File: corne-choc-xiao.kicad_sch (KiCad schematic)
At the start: 46 parts, among them J1 LiPo, Q1 SI2032, SW10 SW_PUSH, SW11 SW_PUSH, SW12 SW_PUSH, SW14 SW_PUSH, SW15 SW_PUSH, SW16 SW_PUSH, SW17 SW_PUSH, SW18 SW_PUSH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

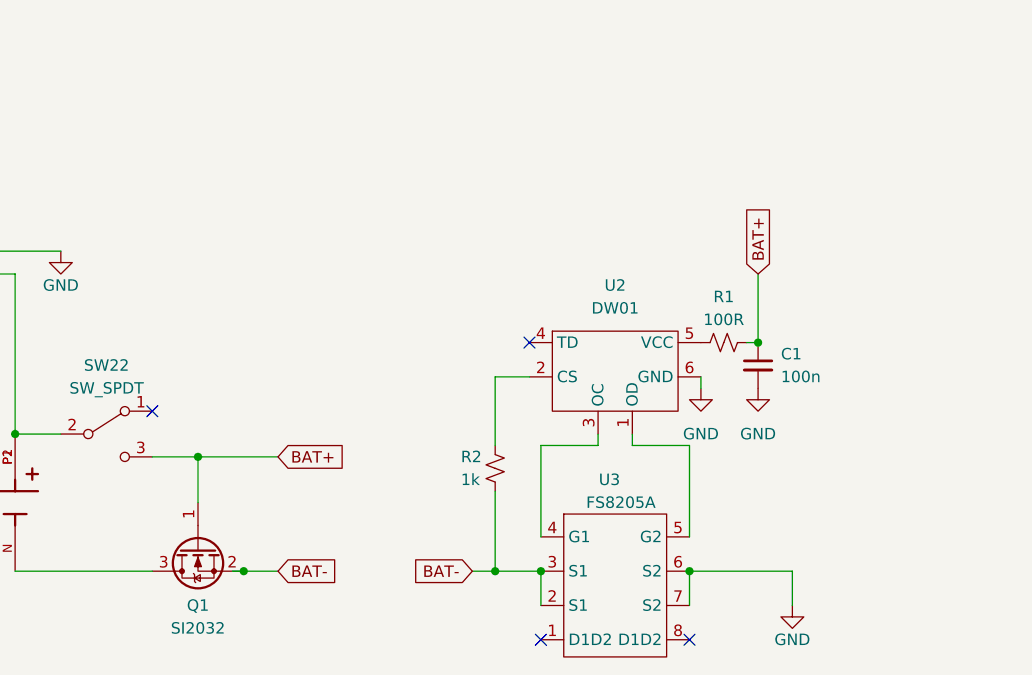
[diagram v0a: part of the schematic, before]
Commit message: fix battery protection circuit
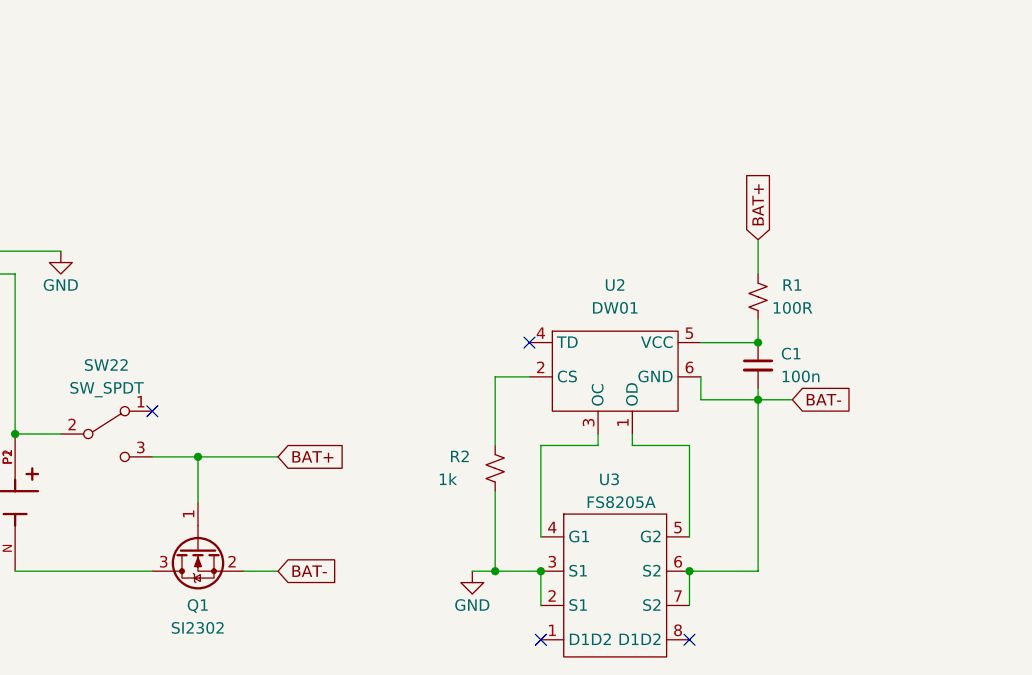
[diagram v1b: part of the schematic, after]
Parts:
- Q1: value SI2032 -> SI2302
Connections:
- net BAT+: no longer C1.1
- net BAT-: now also C1.2, U2.6 (GND), U3.6 (S2), U3.7 (S2); no longer R2.2, U3.2 (S1), U3.3 (S1)
- net GND: now also R2.2, U3.2 (S1), U3.3 (S1); no longer C1.2, U2.6 (GND), U3.6 (S2), U3.7 (S2)
- net at R1.1, U2.5 (VCC): now also C1.1
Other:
- moved on the sheet: R1

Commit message: added readme and ibom
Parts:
- renumbered SW22 to S1
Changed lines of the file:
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@@
   (symbol (lib_id "Switch:SW_SPDT") (at 50.8 134.62 0) (unit 1)
     (in_bom yes) (on_board yes) (dnp no) (fields_autoplaced)
-    (property "Reference" "SW22" (at 50.8 127 0)
+    (property "Reference" "S1" (at 50.8 127 0)
       (effects (font (size 1.27 1.27)))
     )
@@
       (project "corne-choc-xiao"
         (path "/6780a9f7-ba75-484b-b2f8-dc6d7b20e867"
-          (reference "SW22") (unit 1)
+          (reference "S1") (unit 1)
         )
       )

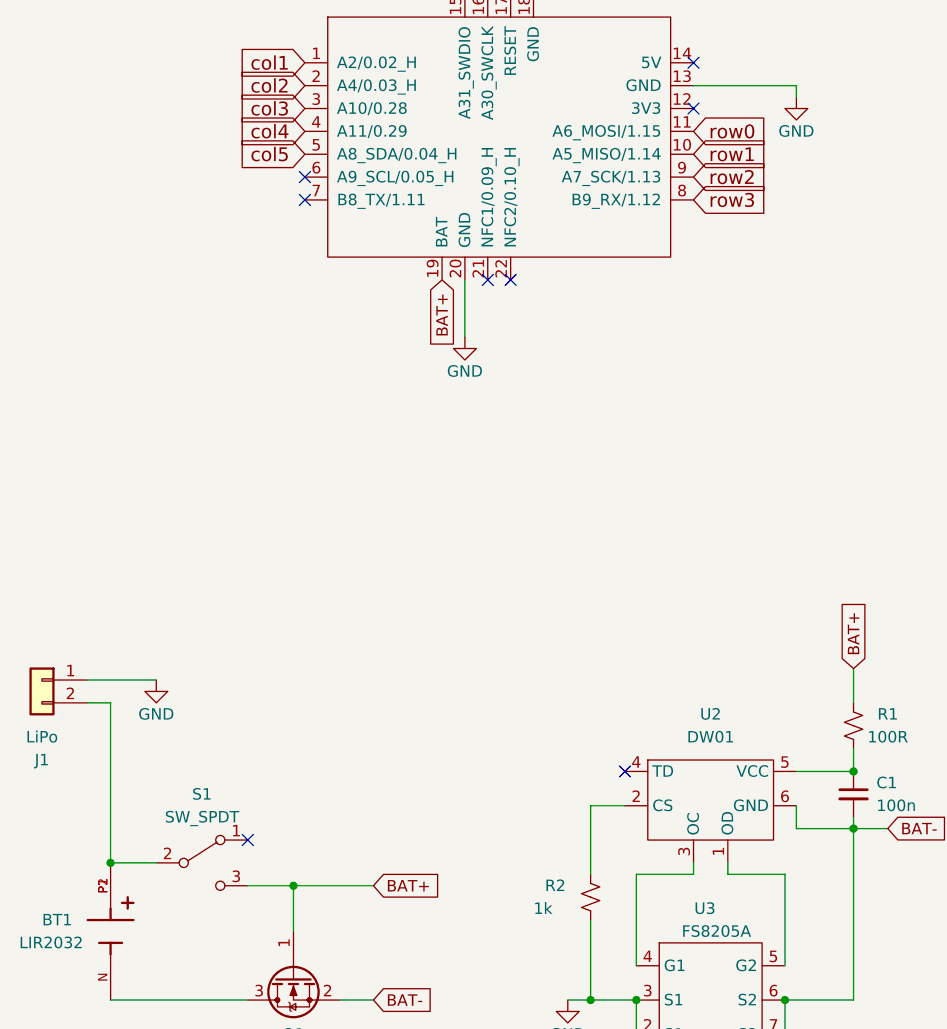
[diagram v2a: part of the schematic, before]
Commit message: added hotswap and removed lipo connector
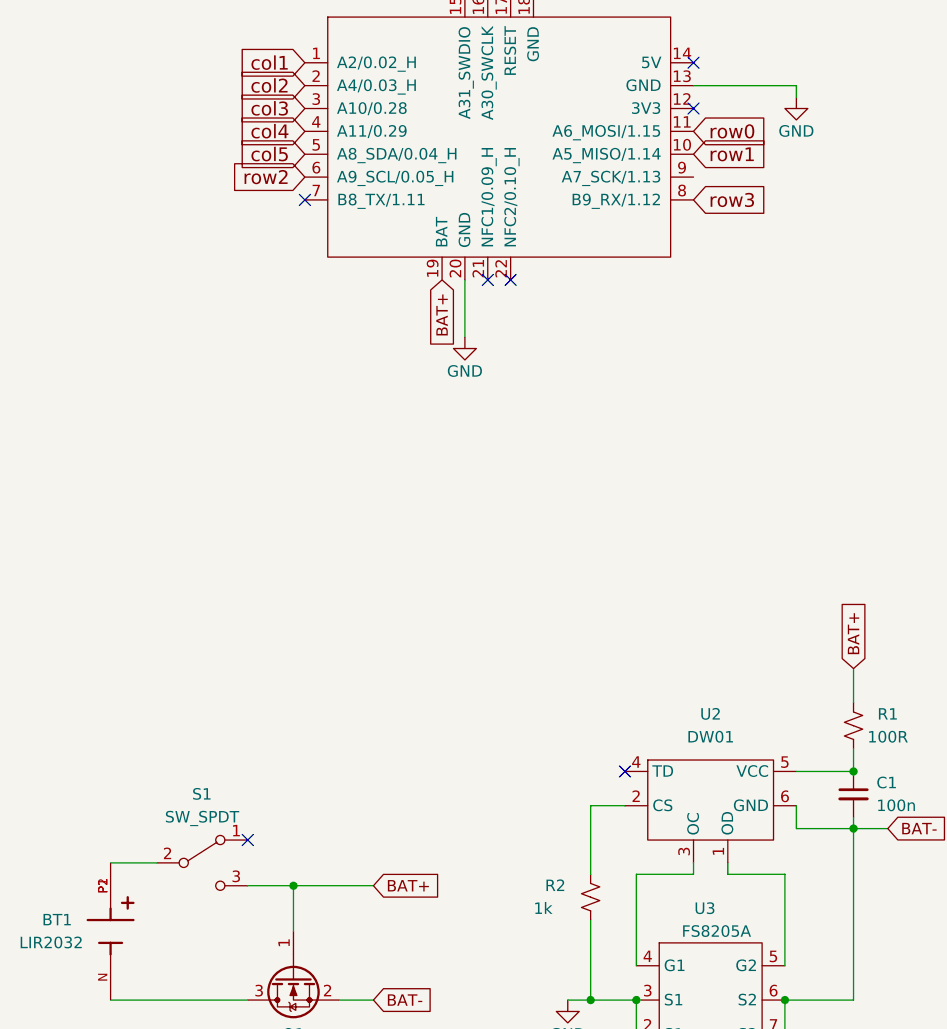
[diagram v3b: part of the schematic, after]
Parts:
- removed J1: LiPo, Connector_JST:JST_GH_SM02B-GHS-TB_1x02-1MP_P1.25mm_Horizontal, symbol Connector_Generic:Conn_01x02
- D10, D11, D12, D14, D15, D16, D17, D18, D19, D2, D20, D21, D3, D4, D5, D6, D8, D9: footprint corne-choc-xiao:D3_TH_SMD_v2 -> corne-choc-xiao:SOD-123-TH
- SW10, SW11, SW12, SW14, SW15, SW16, SW17, SW18, SW19, SW2, SW20, SW21, SW3, SW4, SW5, SW6, SW8, SW9: footprint corne-choc-xiao:choc_socket-rev -> corne-choc-xiao:Kailh_socket_PG1350_optional_reversible
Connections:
- net row2: now also U1.6 (A9_SCL/0.05_H); no longer U1.9 (A7_SCK/1.13)
- no-connect marks 14 -> 13

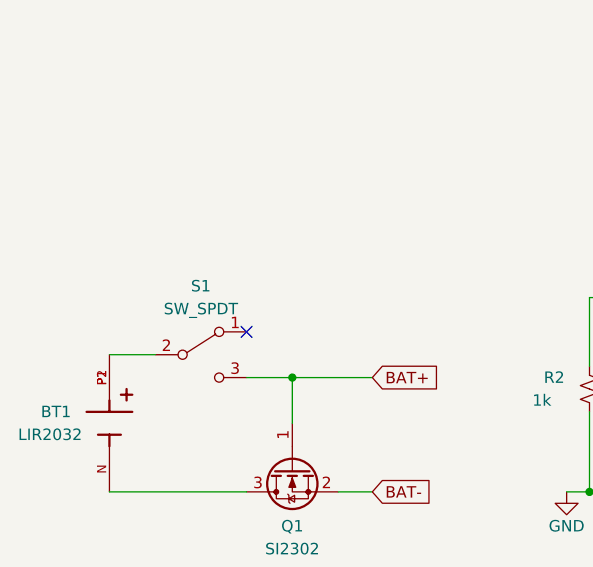
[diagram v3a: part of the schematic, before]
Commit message: readded lipo terminals
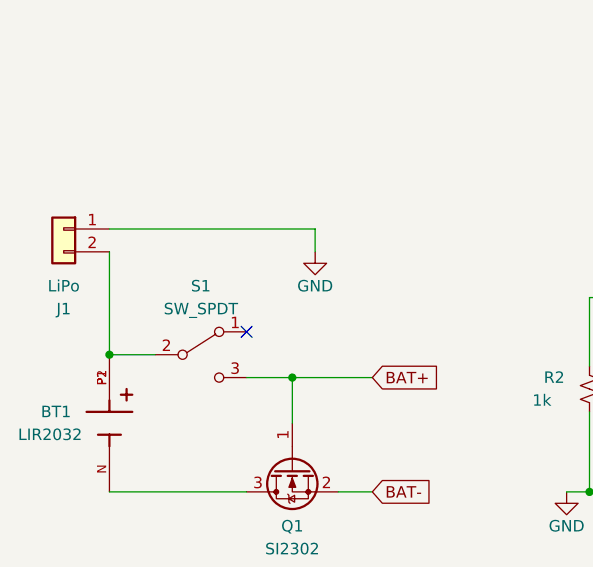
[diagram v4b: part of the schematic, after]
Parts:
- added J1: LiPo, Connector_JST:JST_PH_S2B-PH-K_1x02_P2.00mm_Horizontal, symbol Connector_Generic:Conn_01x02
- BT1: footprint 3002:BAT_3002 -> corne-choc-xiao:BAT_3002
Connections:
- net GND: now also J1.1 (Pin_1)
- net at BT1.P1, BT1.P2, S1.2 (B): now also J1.2 (Pin_2)
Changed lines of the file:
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@@
   (junction (at 257.81 29.21) (diameter 0) (color 0 0 0 0)
+  )
+  (junction (at 40.64 134.62) (diameter 0) (color 0 0 0 0)
   )
   (junction (at 99.06 149.86) (diameter 0) (color 0 0 0 0)
@@
     (stroke (width 0) (type default))
   )
+  (wire (pts (xy 63.5 120.65) (xy 63.5 123.19))
+    (stroke (width 0) (type default))
+  )
   (wire (pts (xy 237.49 82.55) (xy 255.27 82.55))
     (stroke (width 0) (type default))
@@
     (stroke (width 0) (type default))
   )
+  (wire (pts (xy 40.64 120.65) (xy 63.5 120.65))
+    (stroke (width 0) (type default))
+  )
   (wire (pts (xy 116.84 49.53) (xy 116.84 48.26))
     (stroke (width 0) (type default))
@@
   )
   (wire (pts (xy 123.19 130.81) (xy 127 130.81))
+    (stroke (width 0) (type default))
+  )
+  (wire (pts (xy 40.64 123.19) (xy 40.64 134.62))
     (stroke (width 0) (type default))
   )
@@
     )
   )
+  (symbol (lib_id "power:GND") (at 63.5 123.19 0) (unit 1)
+    (in_bom yes) (on_board yes) (dnp no)
+    (property "Reference" "#PWR02" (at 63.5 129.54 0)
+      (effects (font (size 1.27 1.27)) hide)
+    )
+    (property "Value" "GND" (at 63.5 127 0)
+      (effects (font (size 1.27 1.27)))
+    )
+    (property "Footprint" "" (at 63.5 123.19 0)
+      (effects (font (size 1.27 1.27)) hide)
+    )
+    (property "Datasheet" "" (at 63.5 123.19 0)
+      (effects (font (size 1.27 1.27)) hide)
+    )
+    (pin "1")
+    (instances
+      (project "corne-choc-xiao"
+        (path "/6780a9f7-ba75-484b-b2f8-dc6d7b20e867"
+          (reference "#PWR02") (unit 1)
+        )
+      )
+    )
+  )
   (symbol (lib_id "Switch:SW_SPDT") (at 50.8 134.62 0) (unit 1)
     (in_bom yes) (on_board yes) (dnp no) (fields_autoplaced)
@@
       (effects (font (size 1.27 1.27)) (justify left))
     )
-    (property "Footprint" "3002:BAT_3002" (at 40.64 142.24 0)
+    (property "Footprint" "corne-choc-xiao:BAT_3002" (at 40.64 142.24 0)
       (effects (font (size 1.27 1.27)) (justify bottom) hide)
     )
@@
         )
       )
+    )
+  )
+  (symbol (lib_id "Connector_Generic:Conn_01x02") (at 35.56 120.65 0) (mirror y) (unit 1)
+    (in_bom yes) (on_board yes) (dnp no)
+    (property "Reference" "J1" (at 35.56 129.54 0)
+      (effects (font (size 1.27 1.27)))
+    )
+    (property "Value" "LiPo" (at 35.56 127 0)
+      (effects (font (size 1.27 1.27)))
+    )
+    (property "Footprint" "Connector_JST:JST_PH_S2B-PH-K_1x02_P2.00mm_Horizontal" (at 35.56 120.65 0)
+      (effects (font (size 1.27 1.27)) hide)
+    )
+    (property "Datasheet" "~" (at 35.56 120.65 0)
+      (effects (font (size 1.27 1.27)) hide)
+    )
+    (pin "1")
+    (pin "2")
+    (instances
+      (project "corne-choc-xiao"
+        (path "/6780a9f7-ba75-484b-b2f8-dc6d7b20e867"
+          (reference "J1") (unit 1)
+        )
+      )
